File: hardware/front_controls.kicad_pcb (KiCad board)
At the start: 2 copper layers, 99.8 x 99.8 mm, 87 parts, among them J1 Conn_01x02, J2 Conn_01x02, J3 Conn_01x02, J4 Conn_01x02, J5 Conn_01x02, J6 Conn_01x02, J7 Conn_01x02, J8 Conn_01x02, J9 Conn_01x02, P2 CONN_01X10, Q1 Q_PNP_BEC, U1 Adafruit_Metro_Mini, U10 G3VM-31BR, U2 G3VM-31BR, U3 G3VM-31BR, U4 G3VM-31BR, U5 G3VM-31BR, U6 G3VM-31BR, U7 G3VM-31BR, U8 G3VM-31BR, U9 G3VM-31BR

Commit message: Version 2 hardware files
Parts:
- removed D21: D_Schottky, Diode_SMD:D_SMC
- removed Q1: Q_PNP_BEC, Package_TO_SOT_SMD:SOT-23
- removed the R16 at (139.1, 109.2)
- removed the R25 at (93.7, 140.6)
- removed the R26 at (93.7, 138.0)
- removed the R28 at (93.7, 133.0)
- removed the R29 at (93.7, 130.4)
- removed the R31 at (135.9, 73.7)
- removed the R32 at (146.1, 73.7)
- removed the R35 at (176.5, 73.7)
- removed U1: Adafruit_Metro_Mini, Adafruit:DIP-28_W15.24mm
- added A1: Arduino_Nano_v3.x, NANO:Arduino_Nano, F.Cu at (153.9, 97.8)
- added C11: 33pf, Capacitor_SMD:C_0402_1005Metric, F.Cu at (112.5, 127.8)
- added C12: 33pf, Capacitor_SMD:C_0402_1005Metric, F.Cu at (112.5, 123.2)
- added C13: 100nf, Capacitor_SMD:C_0402_1005Metric, F.Cu at (120.6, 111.9)
- added C14: 100nf, Capacitor_SMD:C_0402_1005Metric, F.Cu at (128.5, 116.2)
- added C15: 100nf, Capacitor_SMD:C_0402_1005Metric, F.Cu at (166.7, 105.2)
- added C16: 100nf, Capacitor_SMD:C_0402_1005Metric, F.Cu at (151.2, 87.8)
- added C17: 330uf, Capacitor_THT:CP_Radial_D8.0mm_P3.50mm, F.Cu at (96.2, 95.8)
- added Cboot1: 0.1uf, Capacitor_SMD:C_0402_1005Metric, F.Cu at (109.6, 98.6)
- added Chf1: 220nf, Capacitor_SMD:C_0805_2012Metric, F.Cu at (109.3, 88.9)
- added Cin1: 10uf, Capacitor_SMD:C_0805_2012Metric, F.Cu at (109.5, 86.1)
- added Cout1: 22uF, Capacitor_SMD:C_0805_2012Metric, F.Cu at (100.6, 106.6)
- added Cout2: 22uF, Capacitor_SMD:C_0805_2012Metric, F.Cu at (102.6, 106.6)
- added Cout3: 22uF, Capacitor_SMD:C_0805_2012Metric, F.Cu at (117.6, 106.7)
- added Cout4: 22uF, Capacitor_SMD:C_0805_2012Metric, F.Cu at (115.6, 106.7)
- added J10: Conn_01x02, Connector_PinHeader_2.54mm:PinHeader_1x02_P2.54mm_Vertical, F.Cu at (124.8, 95.4)
- added L1: 8uH, 14m, Inductor_SMD:L_Bourns_SRP7028A_7.3x6.6mm, F.Cu at (108.4, 104.9)
- added P1: PWR, Connector_JST:JST_EH_B2B-EH-A_1x02_P2.50mm_Vertical, F.Cu at (92.0, 83.8)
- added P3: HM-10, Connector_PinSocket_2.54mm:PinSocket_1x06_P2.54mm_Vertical, F.Cu at (128.0, 133.6)
- added P4: Conn_01x06, Connector_PinHeader_2.54mm:PinHeader_1x06_P2.54mm_Vertical, F.Cu at (121.2, 83.4)
- added R0: 500R, Resistor_SMD:R_0402_1005Metric, F.Cu at (173.4, 74.5)
- added R14: 1k, Resistor_SMD:R_0402_1005Metric, F.Cu at (100.6, 122.4)
- added R15: 1k, Resistor_SMD:R_0402_1005Metric, F.Cu at (100.5, 119.6)
- added R17: 100k, Resistor_SMD:R_0402_1005Metric, F.Cu at (169.3, 84.6)
- added R18: 1k, Resistor_SMD:R_0402_1005Metric, F.Cu at (100.6, 129.4)
- added R19: 1k, Resistor_SMD:R_0402_1005Metric, F.Cu at (100.6, 126.4)
- added R20: 1k, Resistor_SMD:R_0402_1005Metric, F.Cu at (107.4, 129.4)
- added R36: 10R, Resistor_SMD:R_0402_1005Metric, F.Cu at (93.7, 128.0)
- added R39: 10R, Resistor_SMD:R_0402_1005Metric, F.Cu at (93.7, 125.4)
- added R4: 500R, Resistor_SMD:R_0402_1005Metric, F.Cu at (132.6, 74.4)
- added R40: 10R, Resistor_SMD:R_0402_1005Metric, F.Cu at (93.7, 122.9)
- added R42: 4K7 1%, Resistor_SMD:R_0402_1005Metric, F.Cu at (165.4, 91.4)
- added R43: 100k, Resistor_SMD:R_0402_1005Metric, F.Cu at (128.0, 117.7)
- added R44: 100k, Resistor_SMD:R_0402_1005Metric, F.Cu at (165.0, 89.6)
- added R5: 500R, Resistor_SMD:R_0402_1005Metric, F.Cu at (122.6, 74.4)
- added R7: 500R, Resistor_SMD:R_0402_1005Metric, F.Cu at (102.7, 74.4)
- added R9: 1k, Resistor_SMD:R_0402_1005Metric, F.Cu at (100.6, 115.4)
- added Rfbb1: 24K9 1%, Resistor_SMD:R_0402_1005Metric, F.Cu at (104.8, 96.3)
- added Rfbt1: 100k 1%, Resistor_SMD:R_0402_1005Metric, F.Cu at (104.8, 99.3)
- added U12: LMR33630ADDA, NANO:Texas_HSOP-8-1EP_3.9x4.9mm_P1.27mm_ThermalVias, F.Cu at (108.3, 94.1)
- added U13: MCP23017-E/SO, Package_SO:SOIC-28W_7.5x18.7mm_P1.27mm, F.Cu at (158.4, 85.8)
- added U14: MCP2515-xSO, Package_SO:SOIC-18W_7.5x11.6mm_P1.27mm, F.Cu at (121.5, 122.1)
- added U15: TJA1051T, Package_SO:SOIC-8_3.9x4.9mm_P1.27mm, F.Cu at (124.8, 111.8)
- added Y1: 12Mhz, Crystal:Crystal_SMD_3225-4Pin_3.2x2.5mm, F.Cu at (112.5, 125.5)
- D1, D14, D15, D16, D17, D18, D19, D2, D3, D4, D5, D6: footprint Diode_SMD:D_SMC -> Diode_SMD:D_SOD-123
- D10, D11, D12, D13, D8, D9: value 4.7 -> 4.7V Zener; footprint Diode_SMD:D_SMB -> Diode_SMD:D_SOD-323
- D20: value D_Schottky -> 15V standoff; footprint Diode_SMD:D_SMC -> Diode_SMD:D_SMB
- D7: value 5.1 -> 5.1V Zener
- R1, R2, R3: value 500 -> 500R
- R10: value 10 -> 1k
- R24, R27: value 10 -> 10R
- R30, R33: value 500 -> 10R
- R34: value 500 -> 100k
- R6: value 1k -> 500R
- R8: value 100k -> 500R
- moved R8 85.4 mm to (93.1, 74.4), turned to 270 degrees
- moved R33 84.5 mm to (93.7, 130.5), turned to 180 degrees
- moved J9 83.5 mm to (93.1, 52.5)
- moved U10 83.5 mm to (93.1, 66.7)
- moved J1 78.2 mm to (173.4, 52.5)
- moved U2 78.2 mm to (173.4, 66.7)
- moved R1 67.9 mm to (163.2, 73.1)
- moved R30 67.5 mm to (93.7, 133.0), turned to 180 degrees
- moved U9 63.7 mm to (102.7, 66.7)
- moved J8 63.7 mm to (102.8, 52.5)
- moved J2 57.8 mm to (163.2, 52.5)
- moved U3 57.8 mm to (163.2, 66.7)
- moved R6 53.0 mm to (112.6, 74.4), turned to 270 degrees
- moved R2 47.7 mm to (153.1, 74.4)
- moved J7 43.7 mm to (112.6, 52.5)
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- renumbered R4 to R12, R7 to R13, R5 to R16, R9 to R21, R12 to R22, R18 to R23, R13 to R25, R19 to R26, R14 to R28, R20 to R29, R15 to R31, R21 to R32, R22 to R35, R17 to R37, R23 to R38, R11 to R41
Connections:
- net Net-(C1-Pad1) renamed /IN_LOW1
- net Net-(C10-Pad1) renamed /IN_HIGH6
- net Net-(C5-Pad1) renamed /IN_HIGH1
- net Net-(C6-Pad1) renamed /IN_HIGH2
- net Net-(C7-Pad1) renamed /IN_HIGH3
- net Net-(C8-Pad1) renamed /IN_HIGH4
- C2 pad 1: Net-(C2-Pad1) -> /IN_LOW2
- C3 pad 1: Net-(C3-Pad1) -> /IN_LOW3
- C4 pad 1: Net-(C4-Pad1) -> /IN_AN1
- C9 pad 1: Net-(C9-Pad1) -> /IN_HIGH5
- D12 pad 1: Net-(C9-Pad1) -> /IN_HIGH5
- D2 pad 2: GND -> Net-(D2-Pad2)
- D20 pad 1: Net-(D20-Pad1) -> GND
- D20 pad 2: Net-(D20-Pad2) -> Net-(C17-Pad1)
- D4 pad 2: GND -> Net-(D4-Pad2)
- D6 pad 2: GND -> Net-(D6-Pad2)
- D7 pad 1: Net-(C4-Pad1) -> /IN_AN1
- P2 pad 10: Net-(D1-Pad1) -> Net-(P2-Pad10)
- P2 pad 8: Net-(D5-Pad1) -> Net-(P2-Pad8)
- P2 pad 9: Net-(D3-Pad1) -> Net-(P2-Pad9)
- R10 pad 1: Net-(P2-Pad7) -> Net-(D2-Pad2)
- R10 pad 2: Net-(C4-Pad1) -> GND
- R16 pad 2: Net-(C2-Pad1) -> /IN_LOW2
- R21 pad 2: Net-(C3-Pad1) -> /IN_LOW3
- R27 pad 1: Net-(D17-Pad1) -> Net-(D15-Pad1)
- R27 pad 2: Net-(P2-Pad4) -> Net-(P2-Pad2)
- R30 pad 1: Net-(R30-Pad1) -> Net-(D16-Pad1)
- R30 pad 2: GND -> Net-(P2-Pad3)
- R33 pad 1: Net-(R33-Pad1) -> Net-(D17-Pad1)
- R33 pad 2: GND -> Net-(P2-Pad4)
- R34 pad 1: Net-(R34-Pad1) -> /IN_HIGH5
- R35 pad 1: Net-(C9-Pad1) -> /IN_HIGH5
- R41 pad 1: Net-(C4-Pad1) -> /IN_AN1
- R6 pad 1: Net-(D5-Pad2) -> Net-(R6-Pad1)
- R6 pad 2: Net-(C3-Pad1) -> GND
- R8 pad 1: VCC -> Net-(R8-Pad1)
- R8 pad 2: Net-(C2-Pad1) -> GND
- U10 pad 1: Net-(U1-Pad13) -> /OUT_U10
- U10 pad 2: Net-(R35-Pad1) -> Net-(R8-Pad1)
- U10 pad 4: Net-(U10-Pad4) -> (no net)
- U2 pad 1: Net-(Q1-Pad2) -> /OUT_U2
- U2 pad 2: Net-(R1-Pad1) -> Net-(R0-Pad1)
- U2 pad 4: Net-(U2-Pad4) -> (no net)
- U3 pad 1: Net-(Q1-Pad1) -> /OUT_U3
- U3 pad 2: Net-(R2-Pad1) -> Net-(R1-Pad1)
- U3 pad 4: Net-(U3-Pad4) -> (no net)
- U4 pad 1: Net-(D20-Pad2) -> /OUT_U4
- U4 pad 2: Net-(R3-Pad1) -> Net-(R2-Pad1)
- U4 pad 4: Net-(U4-Pad4) -> (no net)
- U5 pad 1: Net-(D21-Pad2) -> /OUT_U5
- U5 pad 2: Net-(R30-Pad1) -> Net-(R3-Pad1)
- U5 pad 4: Net-(U5-Pad4) -> (no net)
- U6 pad 1: Net-(U1-Pad9) -> /OUT_U6
- U6 pad 4: Net-(U6-Pad4) -> (no net)
- U7 pad 1: Net-(U1-Pad10) -> /OUT_U7
- U8 pad 1: Net-(U1-Pad11) -> /OUT_U8
- U8 pad 2: Net-(R33-Pad1) -> Net-(R6-Pad1)
- U9 pad 1: Net-(U1-Pad12) -> /OUT_U9
- U9 pad 2: Net-(R34-Pad1) -> Net-(R7-Pad1)
- U9 pad 4: Net-(U9-Pad4) -> (no net)
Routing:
- net Net-(D21-Pad2): track 155.5 -> 0.00 mm, vias 2 -> 0
- net /IN_LOW2: track 0.00 -> 133.4 mm, vias 0 -> 2
- net Net-(U1-Pad9): track 133.2 -> 0.00 mm
- net Net-(U1-Pad10): track 130.3 -> 0.00 mm
- net /IN_LOW3: track 0.00 -> 129.4 mm, vias 0 -> 2
- net Net-(U1-Pad11): track 125.9 -> 0.00 mm
- net Net-(U1-Pad12): track 121.5 -> 0.00 mm
- net VCC: track 92.7 -> 214.1 mm, vias 2 -> 3
- net Net-(U1-Pad13): track 119.9 -> 0.00 mm
- net /IN_AN1: track 0.00 -> 117.5 mm, vias 0 -> 1
- net /BT_EN: track 0.00 -> 114.7 mm, vias 0 -> 1
- net Net-(D20-Pad2): track 111.5 -> 0.00 mm, vias 2 -> 0
- net Net-(Q1-Pad1): track 110.8 -> 0.00 mm
- net Net-(C4-Pad1): track 107.9 -> 0.00 mm, vias 2 -> 0
- net /BT_STATE: track 0.00 -> 102.1 mm, vias 0 -> 1
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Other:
- board size 99.8 x 99.8 mm -> 95 x 95 mm
- board text added: "EDL front_controls V. 0.2.0"
- board text removed: "EDL front_controls V. 0.1.0"

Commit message: Hardware V2 major modifications
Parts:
- removed P4: Conn_01x06, Connector_PinHeader_2.54mm:PinHeader_1x06_P2.54mm_Vertical
- removed U12: LMR33630ADDA, NANO:Texas_HSOP-8-1EP_3.9x4.9mm_P1.27mm_ThermalVias
- added C18: 1 uF, Capacitor_SMD:C_0805_2012Metric, F.Cu at (106.5, 99.0)
- added H3: Expansion, Connector_PinHeader_2.54mm:PinHeader_2x08_P2.54mm_Vertical, F.Cu at (122.3, 89.4)
- added H4: MountingHole, MountingHole:MountingHole_2.7mm_M2.5, F.Cu at (101.0, 74.4)
- added H5: MountingHole, MountingHole:MountingHole_2.7mm_M2.5, F.Cu at (177.0, 74.4)
- added H6: MountingHole, MountingHole:MountingHole_2.7mm_M2.5, F.Cu at (101.0, 90.4)
- added H7: MountingHole, MountingHole:MountingHole_2.7mm_M2.5, F.Cu at (177.0, 90.4)
- added J11: CAN, Connector_JST:JST_EH_B2B-EH-A_1x02_P2.50mm_Vertical, F.Cu at (124.8, 95.4)
- added JP1: Jumper_NO_Small, Jumper:SolderJumper-2_P1.3mm_Open_RoundedPad1.0x1.5mm, B.Cu at (120.9, 95.9)
- added P2: PWR, Connector_JST:JST_EH_B2B-EH-A_1x02_P2.50mm_Vertical, F.Cu at (94.8, 106.0)
- added R11: 4k7, Resistor_SMD:R_0603_1608Metric, F.Cu at (173.4, 107.4)
- added R45: 4k7, Resistor_SMD:R_0603_1608Metric, F.Cu at (175.2, 83.2)
- added R46: 120R, Resistor_SMD:R_0402_1005Metric, F.Cu at (130.6, 97.6)
- added U1: TXB0104PW, Package_SO:TSSOP-14_4.4x5mm_P0.65mm, F.Cu at (124.0, 130.4)
- added U11: LMR33630ADDA, NANO:Texas_HSOP-8-1EP_3.9x4.9mm_P1.27mm_ThermalVias, F.Cu at (108.4, 93.8)
- C4: value .01uf -> .1uf
- J10: value Conn_01x02 -> CAN; footprint Connector_PinHeader_2.54mm:PinHeader_1x02_P2.54mm_Vertical -> Connector_JST:JST_EH_B2B-EH-A_1x02_P2.50mm_Vertical
- R40: value 10R -> 10k; footprint Resistor_SMD:R_0402_1005Metric -> Resistor_SMD:R_0603_1608Metric
- R41: value 1k -> 2k2; footprint Resistor_SMD:R_0402_1005Metric -> Resistor_SMD:R_0603_1608Metric
- moved J10 4.40 mm to (124.8, 99.8), turned to 0 degrees
- moved Rfbt1 2.56 mm to (103.2, 97.3)
- moved H2 2.28 mm to (127.4, 135.8)
- moved U14 1.28 mm to (121.4, 120.8)
- moved C11 1.20 mm to (112.5, 126.6)
- moved C12 1.20 mm to (112.5, 122.0)
- moved C14 1.20 mm to (128.5, 115.0)
- moved R43 1.20 mm to (128.0, 116.5)
- moved Y1 1.20 mm to (112.5, 124.2)
- moved R7 1.08 mm to (103.8, 74.3)
- moved D7 0.53 mm to (96.8, 121.1)
- moved R41 0.48 mm to (172.2, 110.6)
- moved Cboot1 0.36 mm to (109.6, 98.2)
- moved R40 0.27 mm to (94.0, 122.9)
- turned D20 to 180 degrees
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- renumbered P2 to H1, P3 to H2
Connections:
- net /IN_HIGH1 renamed /IN_HORN
- net /IN_HIGH2 renamed /IN_HL_HIGH
- net /IN_HIGH3 renamed /IN_KILL
- net /IN_HIGH4 renamed /IN_RIGHT
- net /IN_HIGH5 renamed /IN_LEFT
- net /IN_HIGH6 renamed /IN_BRAKE
- net /IN_LOW1 renamed /IN_CLUTCH
- net /IN_LOW2 renamed /IN_KICK
- net /IN_LOW3 renamed /IN_NEUTRAL
- net /OUT_U10 renamed /OUT_HORN
- net /OUT_U2 renamed /OUT_LEFT
- net /OUT_U3 renamed /OUT_RIGHT
- net /OUT_U4 renamed /OUT_REAR
- net /OUT_U5 renamed /OUT_BRAKE
- net /OUT_U6 renamed /OUT_START_EN
- net /OUT_U7 renamed /OUT_HL_HIGH
- net /OUT_U8 renamed /OUT_HL_LOW
- net /OUT_U9 renamed /OUT_RUNNING
- A1 pad 1: (no net) -> /UART_TX
- A1 pad 10: /BT_RX -> /BT_RX_H
- A1 pad 11: /BT_TX -> /BT_TX_H
- A1 pad 17: (no net) -> /3V3
- A1 pad 19: /OUT_15 -> /MCU_A0
- A1 pad 2: (no net) -> /UART_RX
- A1 pad 21: /OUT_14 -> /MCU_A2
- A1 pad 22: /OUT_13 -> /MCU_A3
- A1 pad 26: /OUT_12 -> /MCU_A7
- A1 pad 9: /OUT_11 -> /MCU_D6
- C17 pad 1: Net-(C17-Pad1) -> /VIN
- Chf1 pad 2: Net-(C17-Pad1) -> /VIN
- Cin1 pad 2: Net-(C17-Pad1) -> /VIN
- D20 pad 1: GND -> /VIN
- D20 pad 2: Net-(C17-Pad1) -> GND
- H2 pad 2: /BT_RX -> /BT_RX_L
- H2 pad 3: /BT_TX -> /BT_TX_L
- L1 pad 1: VCC -> Net-(Cboot1-Pad2)
- L1 pad 2: Net-(Cboot1-Pad1) -> VCC
- P1 pad 1: GND -> (no net)
- P1 pad 2: Net-(C17-Pad1) -> /VIN
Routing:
- net /VIN: track 0.00 -> 97.6 mm, vias 0 -> 1
- net /OUT_15: track 68.2 -> 0.00 mm, vias 2 -> 0
- net /OUT_14: track 63.9 -> 0.00 mm, vias 2 -> 0
- net /OUT_13: track 62.6 -> 0.00 mm, vias 2 -> 0
- net /3V3: track 0.00 -> 61.0 mm, vias 0 -> 2
- net /OUT_11: track 60.3 -> 0.00 mm, vias 1 -> 0
- net /MCU_A0: track 0.00 -> 57.9 mm, vias 0 -> 2
- net /OUT_12: track 56.2 -> 0.00 mm, vias 1 -> 0
- net /MCU_D6: track 0.00 -> 54.1 mm, vias 0 -> 1
- net /BT_TX: track 54.0 -> 0.00 mm, vias 4 -> 0
- net /BT_RX: track 53.4 -> 0.00 mm
- net /MCU_A2: track 0.00 -> 52.7 mm, vias 0 -> 2
- net /MCU_A3: track 0.00 -> 51.3 mm, vias 0 -> 2
- net /BT_RX_H: track 0.00 -> 50.6 mm, vias 0 -> 1
- net /BT_TX_H: track 0.00 -> 50.2 mm, vias 0 -> 3
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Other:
- board text added: "A0"
- board text added: "A2"
- board text added: "A3"
- board text added: "A7"
- board text added: "BRAKE"
- board text added: "BTRX"
- board text added: "BTTX"
- board text added: "Brake"
- board text added: "CAN Terminator"
- board text added: "CAN_H"
- board text added: "CAN_L"
- board text added: "Clutch"
- board text added: "D6"
- board text added: "EN"
- board text added: "GND"
- board text added: "HIGH BEAMS"
- board text added: "HL HIGH"
- board text added: "HORN"
- board text added: "KILL"
- board text added: "Kick"
- board text added: "LEFT"
- board text added: "LOW BEAMS"
- board text added: "Left"
- board text added: "MISO"
- board text added: "MOSI"
- board text added: "Neut"
- board text added: "REAR"
- board text added: "RIGHT"
- board text added: "RUNNING LIGHTS"
- board text added: "RX"
- board text added: "Right"
- board text added: "SCK"
- board text added: "SCL"
- board text added: "SDA"
- board text added: "START_EN"
- board text added: "STAT"
- board text added: "SW V"
- board text added: "TX"
- board text added: "VCC"
- board text added: "VIN"

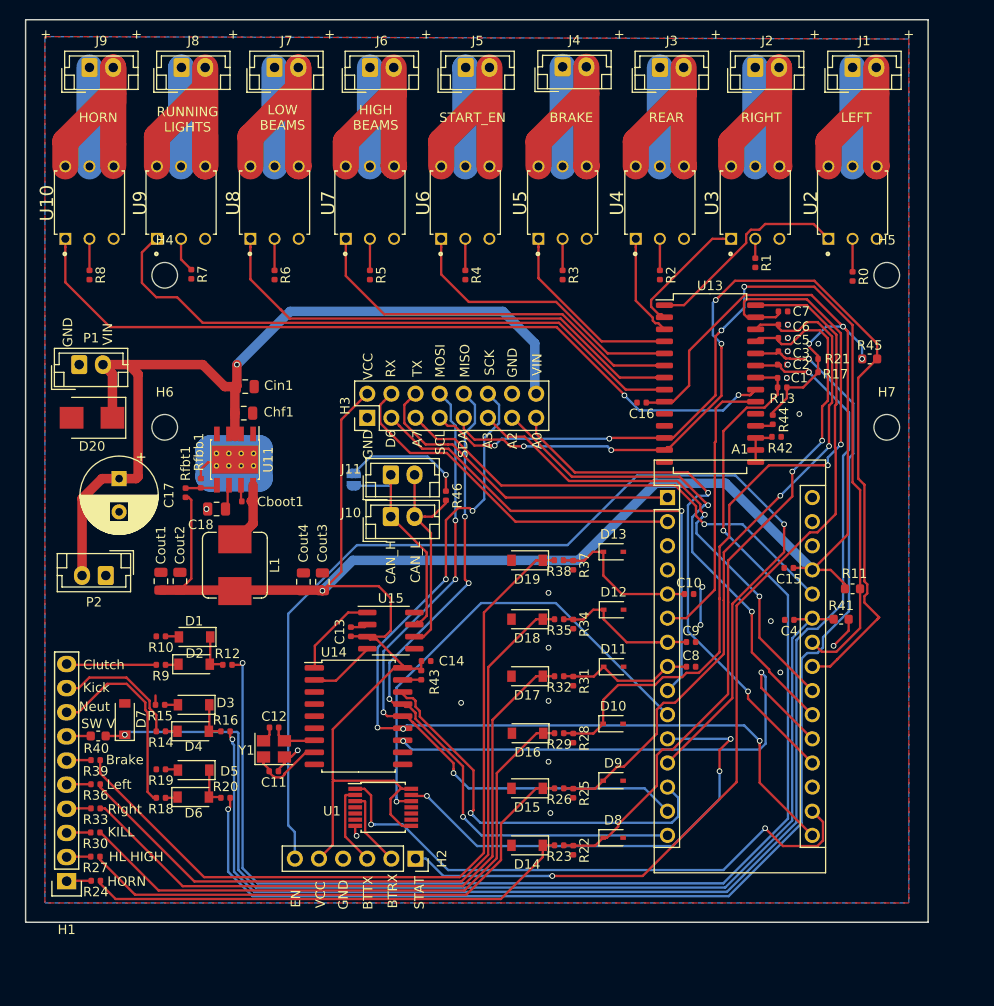
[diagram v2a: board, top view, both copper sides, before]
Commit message: Switched regulators to more available chip
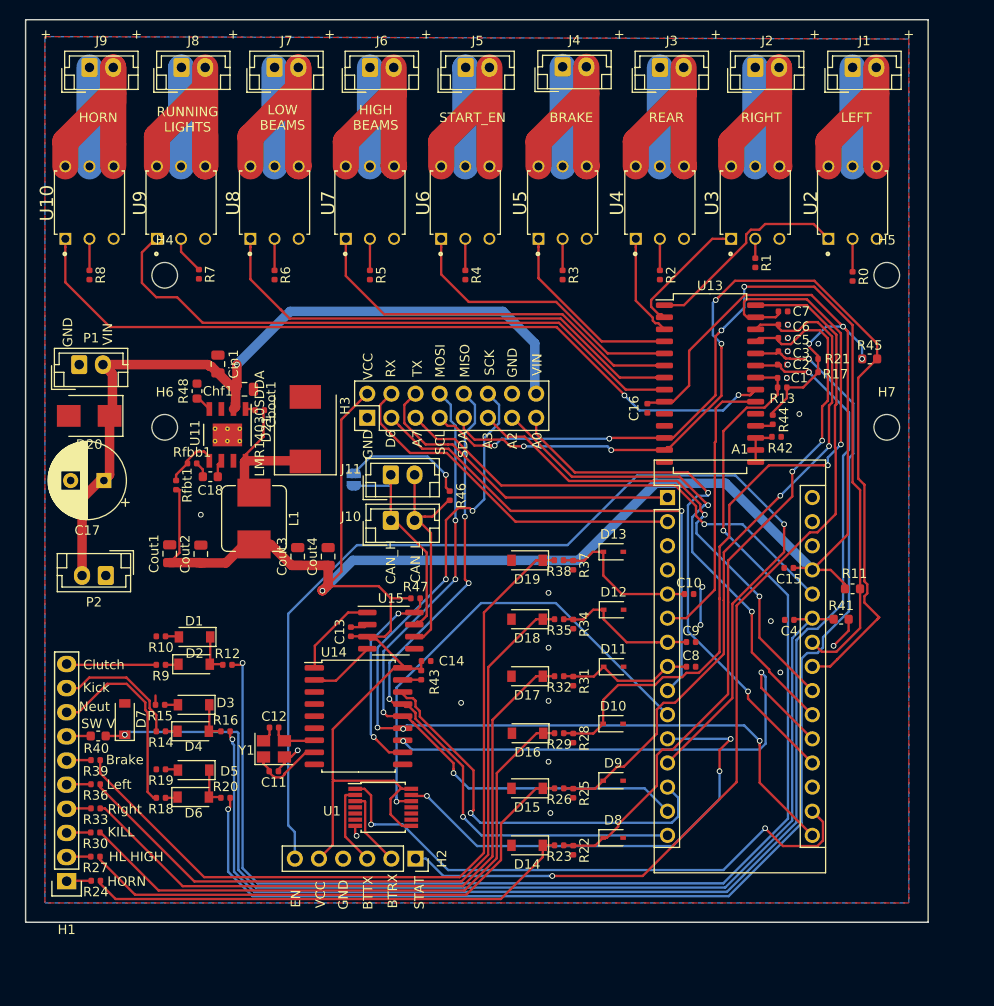
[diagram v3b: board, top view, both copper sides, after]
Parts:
- added D21: 8A, Diode_SMD:D_SMC, F.Cu at (115.8, 90.6)
- added R47: 100k, Resistor_SMD:R_0402_1005Metric, F.Cu at (127.4, 108.4)
- added R48: 62K11, Resistor_SMD:R_0603_1608Metric, F.Cu at (104.4, 86.6)
- C18: value 1 uF -> 22nF; footprint Capacitor_SMD:C_0805_2012Metric -> Capacitor_SMD:C_0603_1608Metric
- L1: value 8uH, 14m -> 8.2uH, 60m
- Rfbb1: value 24K9 1% -> 17k8 1%
- U11: value LMR33630ADDA -> LMR14030SDDA; footprint NANO:Texas_HSOP-8-1EP_3.9x4.9mm_P1.27mm_ThermalVias -> NANO:LMR14030SDDA
- moved Cboot1 9.70 mm to (111.0, 88.6)
- moved L1 5.31 mm to (110.4, 100.0)
- moved Cin1 3.74 mm to (106.6, 83.7), turned to 270 degrees
- moved Cout4 3.72 mm to (118.2, 104.0)
- moved Cout3 3.72 mm to (115.0, 104.0)
- moved Cout2 3.61 mm to (104.8, 103.7)
- moved C18 3.46 mm to (105.8, 95.6)
- moved Cout1 3.04 mm to (101.5, 103.7)
- moved U11 2.72 mm to (107.6, 91.2)
- moved Chf1 2.51 mm to (109.4, 86.4)
- moved Rfbb1 2.28 mm to (103.9, 94.2), turned to 0 degrees
- moved C17 1.61 mm to (94.6, 96.0), turned to 180 degrees
- moved Rfbt1 1.28 mm to (102.2, 96.5)
- moved C16 0.85 mm to (151.8, 88.4), turned to 270 degrees
- moved R7 0.80 mm to (104.6, 74.3)
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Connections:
- P1 pad 1: (no net) -> GND
- U11 pad 1: GND -> Net-(Cboot1-Pad1)
- U11 pad 3: /VIN -> (no net)
- U11 pad 4: (no net) -> Net-(R48-Pad1)
- U11 pad 7: Net-(Cboot1-Pad1) -> GND
- U14 pad 11: (no net) -> /EN_TX
- U15 pad 8: GND -> /EN_TX
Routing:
- net GND: track 41.1 -> 19.5 mm
- net /EN_TX: track 0.00 -> 21.5 mm, vias 0 -> 2
- net /VIN: track 97.6 -> 84.3 mm
- net Net-(Cboot1-Pad2): track 7.73 -> 15.9 mm
- net VCC: track 254.9 -> 259.2 mm
- net Net-(Rfbb1-Pad1): track 3.17 -> 5.95 mm
- net Net-(R48-Pad1): track 0.00 -> 1.75 mm
- net Net-(Cboot1-Pad1): track 1.73 -> 1.06 mm
